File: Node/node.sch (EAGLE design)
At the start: 63 parts, among them J1 U.FL, U2 DW1000-I, U4 ATMEGA328, X2 332-02, Y1 8MHz

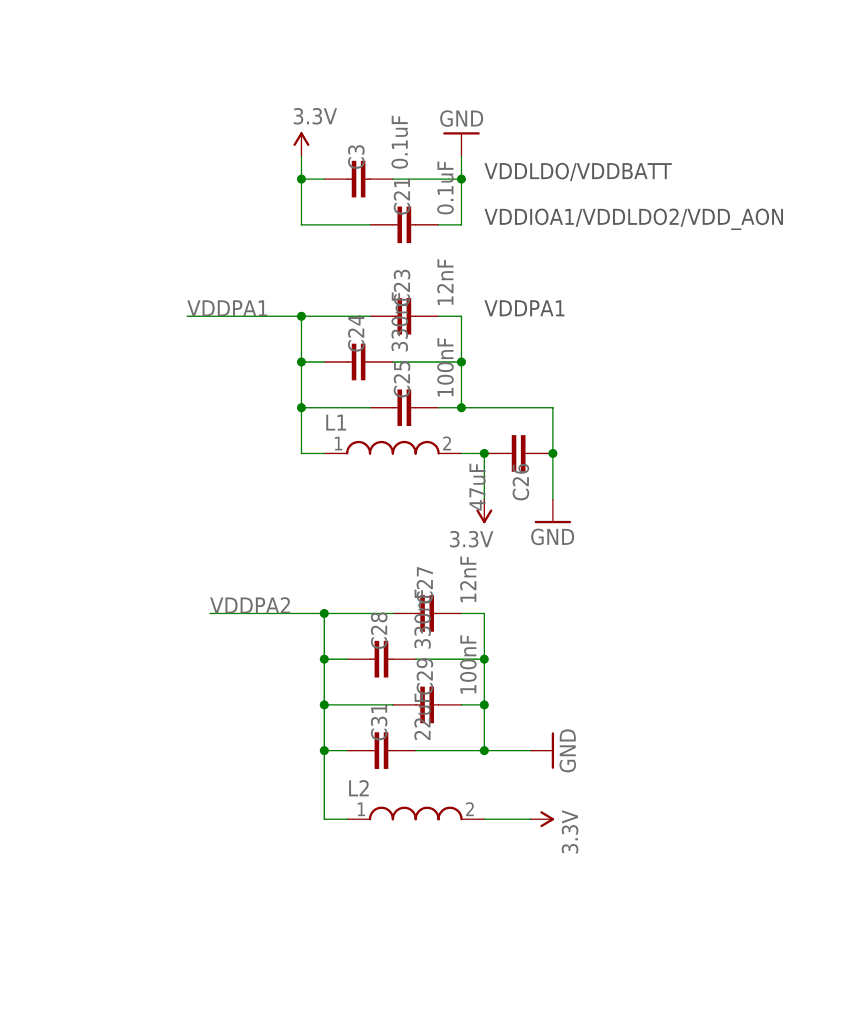
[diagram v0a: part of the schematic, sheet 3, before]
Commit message: Added SCH components for charging and regulation. Calculated resistor values needed for the regulator
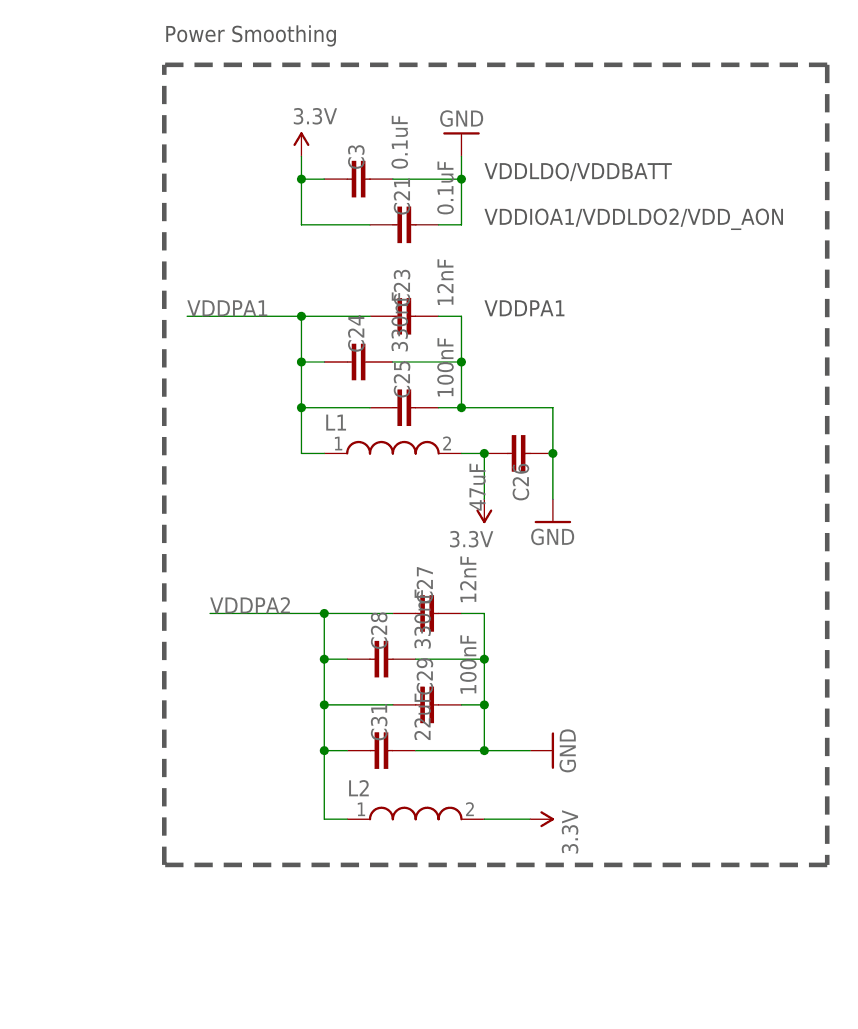
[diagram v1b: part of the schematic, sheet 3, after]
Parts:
- added B1: 1.8-5V, microbuilder:BATTERY
- added C17, C6: 10uF, microbuilder:CAP_CERAMIC0805
- added C22: 10uF, SparkFun-Passives:CAP0805
- added C30: 2.2uF, SparkFun-Passives:CAP0805
- added C32: 0.1uF, SparkFun-Passives:CAP0805
- added C33: 100uF/6V, microbuilder:CAP_TANTALUMB/3528_REFLOW
- added JP1: CHRG, microbuilder:HEADER-1X2
- added JP3: BATT, microbuilder:HEADER-1X2
- added L3: VLC5045-6.8uH - https://www.digikey.com/product-detail/en/e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, microbuilder:INDUCTORTDK_VLC5045
- added LED2: STAT1-ORANGE, microbuilder:LED0805
- added LED3: STAT2-GREEN, microbuilder:LED0805
- added LED4: Power-RED, microbuilder:LED0805
- added PWR: GREEN, microbuilder:LED0805_NOOUTLINE
- added R13, R14, R15: 150, SparkFun-Passives:RESISTOR0805-RES
- added R16: PROG, microbuilder:RESISTOR_DUAL
- added R17: 10K/THERM, adafruit:R-US_FLIPFLOP
- added R22: 1K, SparkFun-Passives:RESISTOR0805-RES
- added R24: 1.15M, SparkFun-Passives:RESISTOR0805-RES
- added R25: 205K, SparkFun-Passives:RESISTOR0805-RES
- added RT1: 1K, adafruit:R-US_R0805
- added RT2: 150K, adafruit:R-US_R0805
- added U1: MCP73833T-AMI/MF, microbuilder:MCP73833DFN
- added U3: TPS61090RSAR, microbuilder:VREG_TPS6103X
- added X1: (no value), microbuilder:TERMBLOCK_1X2
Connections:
- new net 5.0V: C6.P$1, JP1.2, LED2.A, LED3.A, LED4.A, U1.VDD1, U1.VDD2
- new net N$11: LED3.C, R14.2
- new net N$12: R13.1, U1.STAT1
- new net N$13: R14.1, U1.STAT2
- new net N$15: LED4.C, R15.1
- new net N$16: R16.2, U1.PROG
- new net N$17: R15.2, U1.PG
- new net N$18: RT1.1, U1.THERM
- new net N$19: R17.2, RT1.2, RT2.2
- new net N$20: L3.2, U3.SW
- new net N$22: PWR.C, R22.1
- new net N$23: R24.1, R25.2, U3.FB
- new net N$8: LED2.C, R13.2
- new net VBAT: B1.+, C17.P$1, C22.1, C32.1, JP3.2, L3.1, U1.VBAT1, U1.VBAT2, U3.EN, U3.VBAT
- net 3.3V: now also C30.1, C33.+, PWR.A, R24.2, U3.VOUT, X1.2
- net GND: now also B1.-, C17.P$2, C22.2, C30.2, C32.2, C33.-, C6.P$2, JP1.1, JP3.1, R16.1, R17.1, R22.2, R25.1, RT2.1, U1.GND, U3.GND, U3.LBI, U3.PGND, U3.SYNC, X1.1
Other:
- note added: "1.0K = 1000mA"
- note added: "10K = 100mA"
- note added: "10K NTC Thermistor"
- note added: "2.0K = 500mA"
- note added: "5.0K = 200mA"
- note added: "6.8uH power w/2A current"
- note added: "No Thermistor"
- note added: "Power Smoothing"
- note added: "R2 < 500K R1 = 5.5*R2 (3.2V LBO)"
- note added: "R4 = 200K R3 = 1.85Mohm"
- note added: "RT1 = 0 RT2 = NC THERM=10K"
- note added: "RT1 = TBD RT2 = TBD"
- note added: "See Pg 15 1st para"
- note added: "VOUT = 3.3049V"

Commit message: Added the inductor Lib item. Also made a few changes to the ATMEGA Pin assignments to match the breadboarded Radio/Arduino setup
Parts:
- removed L3: VLC5045-6.8uH - https://www.digikey.com/product-detail/en/e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, microbuilder:INDUCTORTDK_VLC5045
- added L4: https://www.digikey.com/product-detail/en/eaton-electronics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, MainLib:DR73-6R8-R
- added R18, R19: 470, SparkFun-Passives:RESISTOR0402-RES
- added RXOK, SFD: (no value), SparkFun-LED:LED0603
- C33: value 100uF/6V -> 100uF/6V - https://www.digikey.com/product-detail/en/avx-corporation/F930G107MBA/478-8135-1-ND/4005827
- R12, R5: device SparkFun-Passives:RESISTOR0805-RES -> SparkFun-Passives:RESISTOR0402-RES
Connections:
- net A4 renamed SDA
- net A5 renamed SCL
- removed net D7: U4.PD7(AIN1)
- new net DWRST: SJ1.1, U4.PB1(OC1A)
- new net N$21: R18.2, SFD.A
- new net N$24: R19.2, RXOK.A
- net !SPICS: now also U4.PB2(SS/OC1B); no longer U4.PD2(INT0)
- net BLU: now also U4.PD3(INT1); no longer U4.PB2(SS/OC1B)
- net D4: no longer SJ1.1
- net GND: now also RXOK.C, SFD.C
- net GPIO0: now also R19.1
- net GPIO1: now also R18.1
- net GRN: now also U4.PD5(T1); no longer U4.PB1(OC1A)
- net IQR: now also U4.PD2(INT0); no longer U4.PD3(INT1)
- net N$20: now also L4.2; no longer L3.2
- net VBAT: now also L4.1; no longer L3.1
- net WAKEUP: now also U4.PD7(AIN1); no longer U4.PD5(T1)
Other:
- note added: "R25 = 205K R24 = 1.15Mohm"
- note removed: "R2 < 500K R1 = 5.5*R2 (3.2V LBO)"
- note removed: "R4 = 200K R3 = 1.85Mohm"
- moved on the sheet: B1, R7

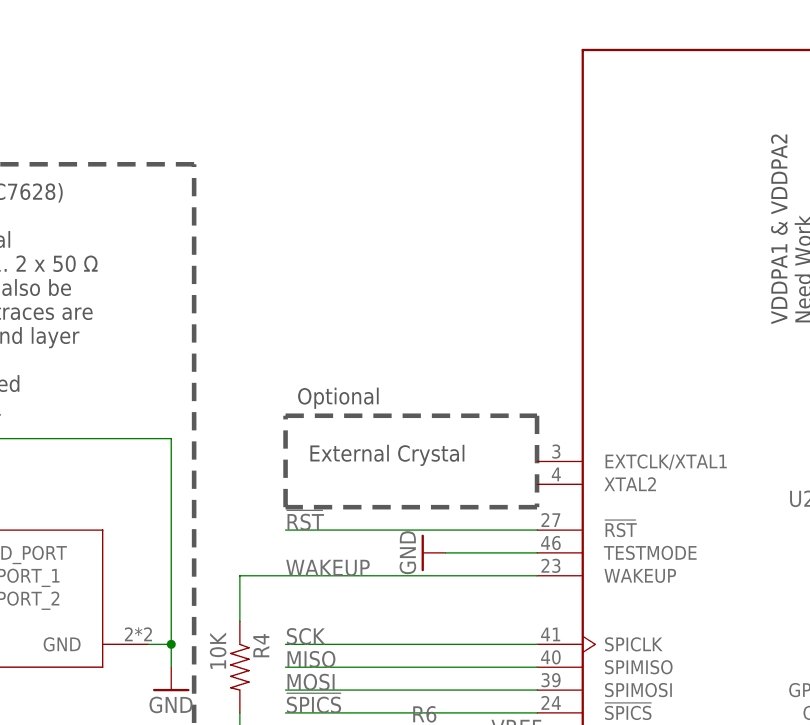
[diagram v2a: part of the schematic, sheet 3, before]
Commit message: Added external TCXO Oscillator to schematic
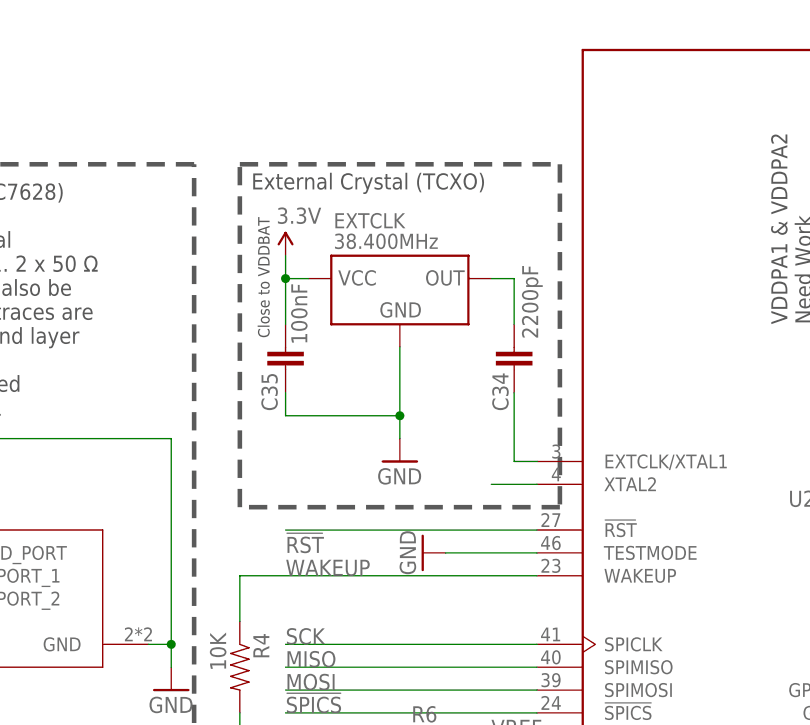
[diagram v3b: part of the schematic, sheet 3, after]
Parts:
- added C34: 2200pF, SparkFun-Passives:CAP0402-CAP
- added C35: 100nF, SparkFun-Passives:CAP0402-CAP
- added EXTCLK: 38.400MHz, MainLib:ASTXR-12
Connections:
- new net N$25: C34.1, U2.EXTCLK/XTAL1
- new net N$26: C34.2, EXTCLK.OUT
- new net N$27: U2.XTAL2
- net 3.3V: now also C35.2, EXTCLK.VCC
- net GND: now also C35.1, EXTCLK.GND
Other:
- note added: "Close to VDDBAT"
- note added: "External Crystal (TCXO)"
- note removed: "External Crystal"
- note removed: "Optional"
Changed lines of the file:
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@@
 <part name="SFD" library="SparkFun-LED" deviceset="LED" device="0603"/>
 <part name="RXOK" library="SparkFun-LED" deviceset="LED" device="0603"/>
+<part name="EXTCLK" library="MainLib" deviceset="ASTXR-12" device="" value="38.400MHz"/>
+<part name="GND17" library="SparkFun-Aesthetics" deviceset="GND" device=""/>
+<part name="C34" library="SparkFun-Passives" deviceset="CAP" device="0402-CAP" value="2200pF"/>
+<part name="SUPPLY10" library="SparkFun-Aesthetics" deviceset="3.3V" device=""/>
+<part name="C35" library="SparkFun-Passives" deviceset="CAP" device="0402-CAP" value="100nF"/>
 </parts>
 <sheets>
@@
 <text x="231.14" y="60.96" size="1.778" layer="97" rot="R90">Optional: Depends
 on SPI Config</text>
-<text x="85.09" y="113.03" size="1.778" layer="97">Optional</text>
 <text x="142.24" y="121.92" size="1.778" layer="97" rot="R90">VDDPA1 &amp; VDDPA2
 Need Work</text>
@@
 <text x="43.18" y="63.5" size="1.778" layer="97">50 Ω </text>
 <text x="43.18" y="71.12" size="1.778" layer="97">50 Ω </text>
-<wire x1="111.76" y1="101.6" x2="83.82" y2="101.6" width="0.508" layer="97" style="longdash"/>
-<wire x1="83.82" y1="101.6" x2="83.82" y2="111.76" width="0.508" layer="97" style="longdash"/>
-<wire x1="83.82" y1="111.76" x2="111.76" y2="111.76" width="0.508" layer="97" style="longdash"/>
-<wire x1="111.76" y1="111.76" x2="111.76" y2="101.6" width="0.508" layer="97" style="longdash"/>
+<wire x1="114.3" y1="101.6" x2="78.74" y2="101.6" width="0.508" layer="97" style="longdash"/>
+<wire x1="78.74" y1="101.6" x2="78.74" y2="139.7" width="0.508" layer="97" style="longdash"/>
+<wire x1="78.74" y1="139.7" x2="114.3" y2="139.7" width="0.508" layer="97" style="longdash"/>
+<wire x1="114.3" y1="139.7" x2="114.3" y2="101.6" width="0.508" layer="97" style="longdash"/>
 <wire x1="213.36" y1="134.62" x2="271.78" y2="134.62" width="0.508" layer="97" style="longdash"/>
 <wire x1="271.78" y1="134.62" x2="271.78" y2="160.02" width="0.508" layer="97" style="longdash"/>
 <wire x1="271.78" y1="160.02" x2="213.36" y2="160.02" width="0.508" layer="97" style="longdash"/>
 <wire x1="213.36" y1="160.02" x2="213.36" y2="134.62" width="0.508" layer="97" style="longdash"/>
-<text x="86.36" y="106.68" size="1.778" layer="97">External Crystal</text>
+<text x="80.01" y="136.906" size="1.778" layer="97">External Crystal (TCXO)</text>
 <text x="330.2" y="144.78" size="1.778" layer="97">VDDLDO/VDDBATT</text>
 <text x="330.2" y="139.7" size="1.778" layer="97">VDDIOA1/VDDLDO2/VDD_AON</text>
@@
 <wire x1="294.64" y1="68.58" x2="294.64" y2="157.48" width="0.508" layer="97" style="longdash"/>
 <text x="294.64" y="160.02" size="1.778" layer="97">Power Smoothing</text>
+<text x="82.042" y="120.396" size="1.27" layer="97" rot="R90">Close to VDDBAT</text>
 </plain>
 <instances>
@@
 <attribute name="NAME" x="206.756" y="38.608" size="1.778" layer="95" rot="R90"/>
 <attribute name="VALUE" x="208.915" y="38.608" size="1.778" layer="96" rot="R90"/>
+</instance>
+<instance part="EXTCLK" gate="G$1" x="96.52" y="124.46" smashed="yes">
+<attribute name="NAME" x="89.154" y="132.588" size="1.6764" layer="95"/>
+<attribute name="VALUE" x="89.154" y="130.302" size="1.6764" layer="95"/>
+</instance>
+<instance part="GND17" gate="1" x="96.52" y="106.68" smashed="yes">
+<attribute name="VALUE" x="93.98" y="104.14" size="1.778" layer="96"/>
+</instance>
+<instance part="C34" gate="G$1" x="109.22" y="119.38" smashed="yes" rot="R180">
+<attribute name="NAME" x="106.807" y="116.586" size="1.778" layer="95" rot="R270"/>
+<attribute name="VALUE" x="110.109" y="128.524" size="1.778" layer="96" rot="R270"/>
+</instance>
+<instance part="SUPPLY10" gate="G$1" x="83.82" y="129.54" smashed="yes">
+<attribute name="VALUE" x="82.804" y="133.096" size="1.778" layer="96"/>
+</instance>
+<instance part="C35" gate="G$1" x="83.82" y="119.38" smashed="yes" rot="R180">
+<attribute name="NAME" x="81.153" y="116.586" size="1.778" layer="95" rot="R270"/>
+<attribute name="VALUE" x="84.455" y="126.492" size="1.778" layer="96" rot="R270"/>
 </instance>
 </instances>
@@
 <junction x="195.58" y="33.02"/>
 </segment>
+<segment>
+<pinref part="EXTCLK" gate="G$1" pin="GND"/>
+<wire x1="96.52" y1="119.38" x2="96.52" y2="111.76" width="0.1524" layer="91"/>
+<pinref part="GND17" gate="1" pin="GND"/>
+<pinref part="C35" gate="G$1" pin="1"/>
+<wire x1="96.52" y1="111.76" x2="96.52" y2="109.22" width="0.1524" layer="91"/>
+<wire x1="83.82" y1="114.3" x2="83.82" y2="111.76" width="0.1524" layer="91"/>
+<wire x1="83.82" y1="111.76" x2="96.52" y2="111.76" width="0.1524" layer="91"/>
+<junction x="96.52" y="111.76"/>
+</segment>
 </net>
 <net name="3.3V" class="0">
@@
 <pinref part="L2" gate="G$1" pin="2"/>
 </segment>
+<segment>
+<pinref part="EXTCLK" gate="G$1" pin="VCC"/>
+<wire x1="86.36" y1="127" x2="83.82" y2="127" width="0.1524" layer="91"/>
+<wire x1="83.82" y1="127" x2="83.82" y2="129.54" width="0.1524" layer="91"/>
+<pinref part="SUPPLY10" gate="G$1" pin="3.3V"/>
+<pinref part="C35" gate="G$1" pin="2"/>
+<wire x1="83.82" y1="127" x2="83.82" y2="121.92" width="0.1524" layer="91"/>
+<junction x="83.82" y="127"/>
+</segment>
 </net>
 <net name="VREF" class="0">
@@
 <pinref part="U2" gate="G$1" pin="!RST"/>
 <wire x1="111.76" y1="99.06" x2="83.82" y2="99.06" width="0.1524" layer="91"/>
-<label x="83.82" y="99.06" size="1.778" layer="95"/>
+<label x="83.82" y="96.52" size="1.778" layer="95"/>
 </segment>
 </net>
@@
 </segment>
 </net>
+<net name="N$25" class="0">
+<segment>
+<pinref part="U2" gate="G$1" pin="EXTCLK/XTAL1"/>
+<wire x1="111.76" y1="106.68" x2="109.22" y2="106.68" width="0.1524" layer="91"/>
+<pinref part="C34" gate="G$1" pin="1"/>
+<wire x1="109.22" y1="114.3" x2="109.22" y2="106.68" width="0.1524" layer="91"/>
+</segment>
+</net>
+<net name="N$26" class="0">
+<segment>
+<pinref part="EXTCLK" gate="G$1" pin="OUT"/>
+<wire x1="109.22" y1="127" x2="106.68" y2="127" width="0.1524" layer="91"/>
+<pinref part="C34" gate="G$1" pin="2"/>
+<wire x1="109.22" y1="127" x2="109.22" y2="121.92" width="0.1524" layer="91"/>
+</segment>
+</net>
+<net name="N$27" class="0">
+<segment>
+<pinref part="U2" gate="G$1" pin="XTAL2"/>
+<wire x1="111.76" y1="104.14" x2="106.68" y2="104.14" width="0.1524" layer="91"/>
+</segment>
+</net>

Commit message: RF work, framing, and finish layer
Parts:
- J1: device SparkFun-Connectors:U.FL -> adafruit:ANTENNA_U.FL
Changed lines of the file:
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@@
 <part name="GND14" library="SparkFun-Aesthetics" deviceset="GND" device=""/>
 <part name="GND15" library="SparkFun-Aesthetics" deviceset="GND" device=""/>
-<part name="J1" library="SparkFun-Connectors" deviceset="U.FL" device="" value="U.FL"/>
+<part name="J1" library="adafruit" library_urn="urn:adsk.eagle:library:420" deviceset="ANTENNA_U.FL" device="" package3d_urn="urn:adsk.eagle:package:6240943/1" value="U.FL"/>
 <part name="TP1" library="SparkFun-Passives" deviceset="TEST-POINT" device="3X4"/>
 <part name="TP2" library="SparkFun-Passives" deviceset="TEST-POINT" device="3X4"/>
